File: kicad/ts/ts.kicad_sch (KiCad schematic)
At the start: 1 part, among them J2 C96ABC

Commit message: Schemativ corrections, work started on pcb
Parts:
- J2: footprint Connector_DIN:DIN41612_R_3x32_Male_Horizontal_THT -> Cobra_original:DIN41612_R_3x32_Male_Horizontal_THT
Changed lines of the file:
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@@
 			)
 		)
-		(property "Footprint" "Connector_DIN:DIN41612_R_3x32_Male_Horizontal_THT"
+		(property "Footprint" "Cobra_original:DIN41612_R_3x32_Male_Horizontal_THT"
 			(at 29.21 149.225 0)
 			(effects

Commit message: Schematic corrections, more traces to pcb, update to DIN 3x32 connector footprint
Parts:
- J2: footprint Cobra_original:DIN41612_R_3x32_Male_Horizontal_THT -> Cobra_original:DIN41612_R_3x32_Male_Horizontal_THT_REV
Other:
- sheet TIMING & CTRL ports: added ~{IORD}; removed none
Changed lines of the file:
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@@
 	(wire
 		(pts
+			(xy 81.28 123.825) (xy 90.805 123.825)
+		)
+		(stroke
+			(width 0)
+			(type default)
+		)
+	)
+	(wire
+		(pts
 			(xy 36.83 76.835) (xy 42.545 76.835)
 		)
@@
 		)
 	)
+	(label "~{IORD}"
+		(at 90.805 123.825 180)
+		(fields_autoplaced yes)
+		(effects
+			(font
+				(size 1.27 1.27)
+			)
+			(justify right bottom)
+		)
+	)
 	(label "A0"
 		(at 42.545 153.035 180)
@@
 			)
 		)
-		(property "Footprint" "Cobra_original:DIN41612_R_3x32_Male_Horizontal_THT"
+		(property "Footprint" "Cobra_original:DIN41612_R_3x32_Male_Horizontal_THT_REV"
 			(at 29.21 149.225 0)
 			(effects
@@
 			(effects
 				(font
+					(size 1.27 1.27)
+				)
+				(justify right)
+			)
+		)
+		(pin "~{IORD}" output
+			(at 81.28 123.825 0)
+			(effects
+				(font

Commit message: Schematic corrections, more traces to pcb
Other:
- sheet TIMING & CTRL ports: added CK, SM; removed none
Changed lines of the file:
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@@
 	(wire
 		(pts
+			(xy 81.28 153.035) (xy 88.265 153.035)
+		)
+		(stroke
+			(width 0)
+			(type default)
+		)
+	)
+	(wire
+		(pts
 			(xy 86.36 185.42) (xy 158.75 185.42)
 		)
@@
 	(wire
 		(pts
+			(xy 81.28 144.78) (xy 88.265 144.78)
+		)
+		(stroke
+			(width 0)
+			(type default)
+		)
+	)
+	(wire
+		(pts
 			(xy 36.83 216.535) (xy 42.545 216.535)
 		)
@@
 	)
 	(label "SM"
+		(at 88.265 144.78 180)
+		(fields_autoplaced yes)
+		(effects
+			(font
+				(size 1.27 1.27)
+			)
+			(justify right bottom)
+		)
+	)
+	(label "SM"
 		(at 42.545 120.015 180)
 		(fields_autoplaced yes)
@@
 		)
 	)
+	(label "CK"
+		(at 88.265 153.035 180)
+		(fields_autoplaced yes)
+		(effects
+			(font
+				(size 1.27 1.27)
+			)
+			(justify right bottom)
+		)
+	)
 	(label "~{MREQ}"
 		(at 133.985 92.075 180)
@@
 			(effects
 				(font
+					(size 1.27 1.27)
+				)
+				(justify right)
+			)
+		)
+		(pin "SM" output
+			(at 81.28 144.78 0)
+			(effects
+				(font
+					(size 1.27 1.27)
+				)
+				(justify right)
+			)
+		)
+		(pin "CK" output
+			(at 81.28 153.035 0)
+			(effects
+				(font

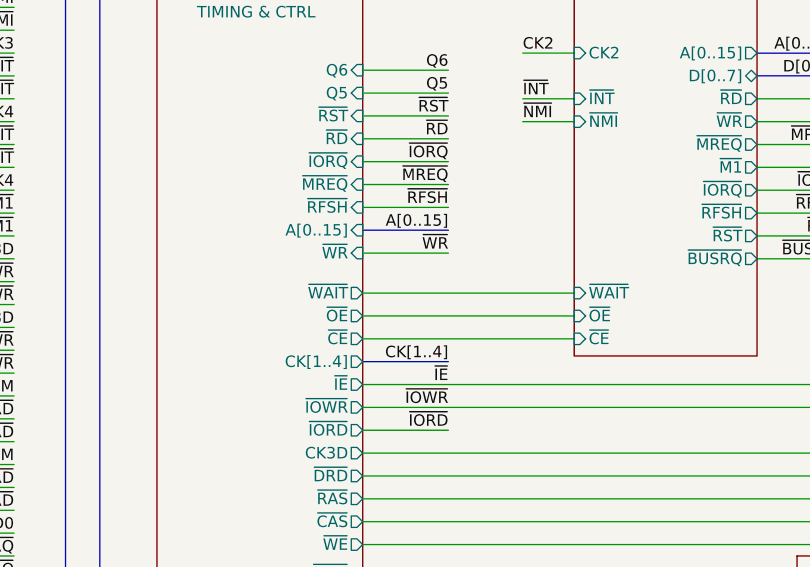
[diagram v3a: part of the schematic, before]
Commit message: 4164 footprint corrected, more pcb traces
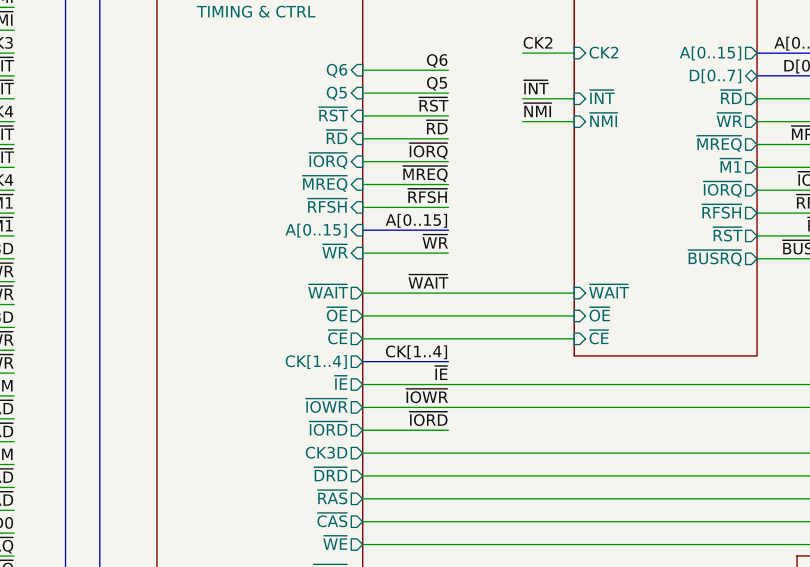
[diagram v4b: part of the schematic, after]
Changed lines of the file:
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@@
+		)
+	)
+	(label "~{WAIT}"
+		(at 90.805 108.585 180)
+		(fields_autoplaced yes)
+		(effects
+			(font
+				(size 1.27 1.27)
+			)
+			(justify right bottom)
 		)
 	)
